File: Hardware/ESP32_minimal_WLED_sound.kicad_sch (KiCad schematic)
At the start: 50 parts, among them J1 Conn_01x04_Male, J2 USB_C_Receptacle_USB2.0, J3 Conn_01x02_Male, J4 Barrel_Jack_Switch_Pin3Ring, J5 Conn_01x03_Male, J6 Conn_01x03_Male, J7 Conn_01x03_Male, J8 Conn_01x02_Male, J9 Conn_01x03_Male, Q1 AO3400A, SW2 Boot, U1 LM1117-5, U2 INA226, U3 LM1117-3.3, U4 TXS0102DCT, U5 ESP32-WROOM-32

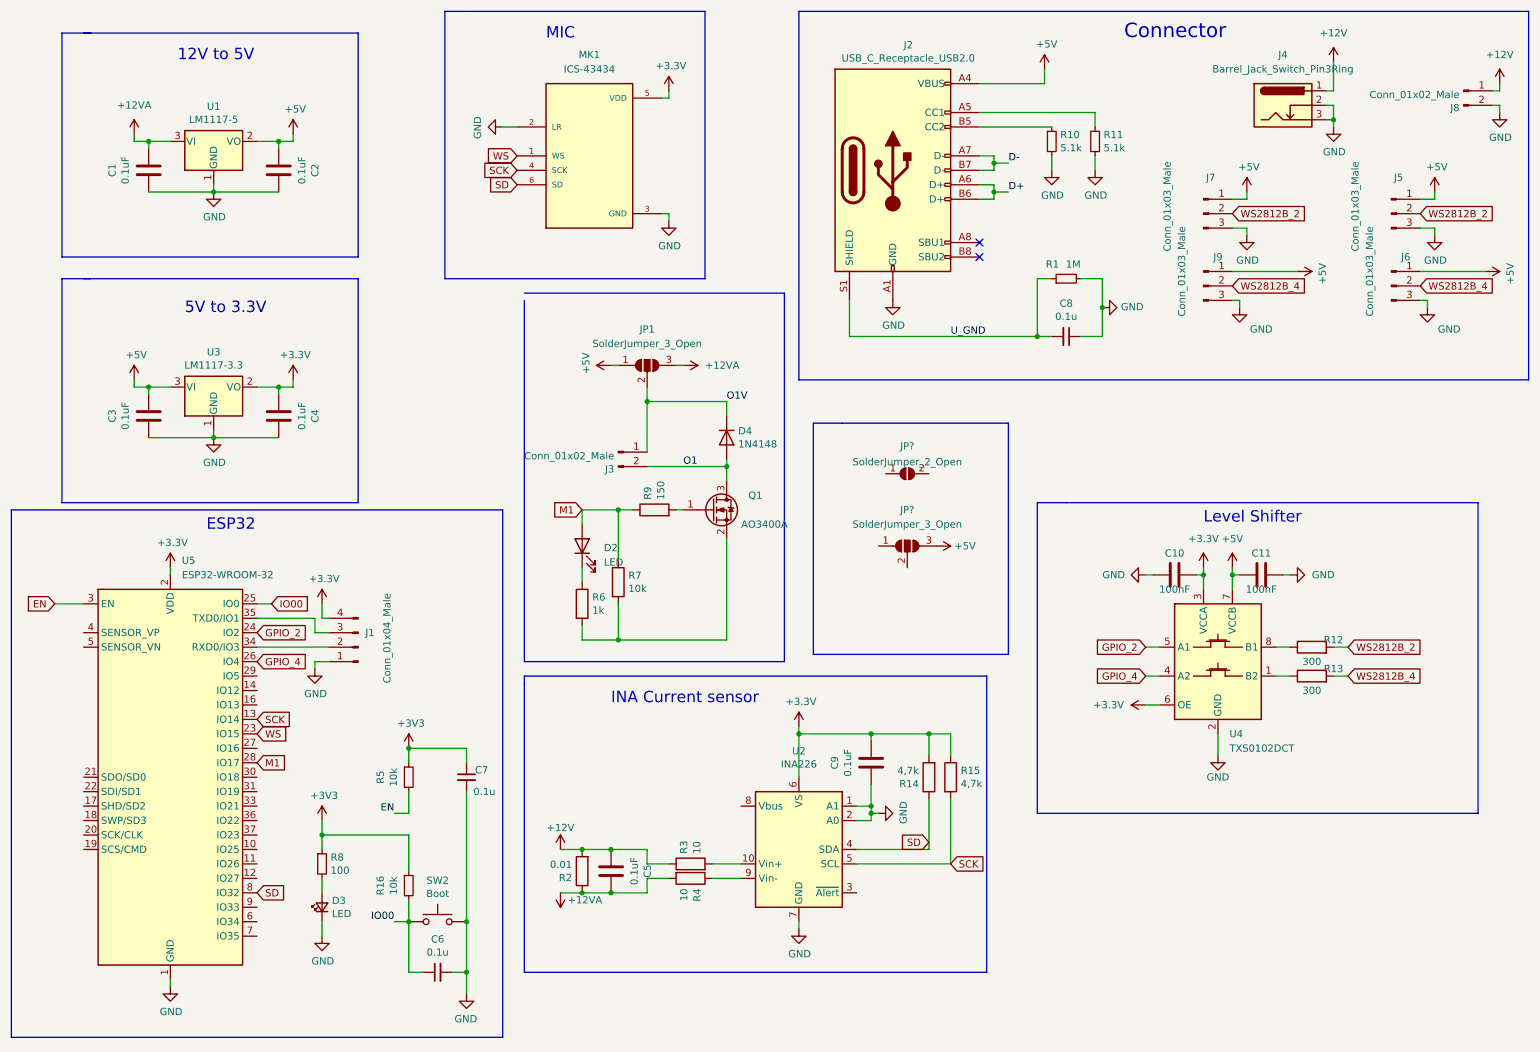
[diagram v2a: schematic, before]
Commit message: switch 12V to 5V to DCDC
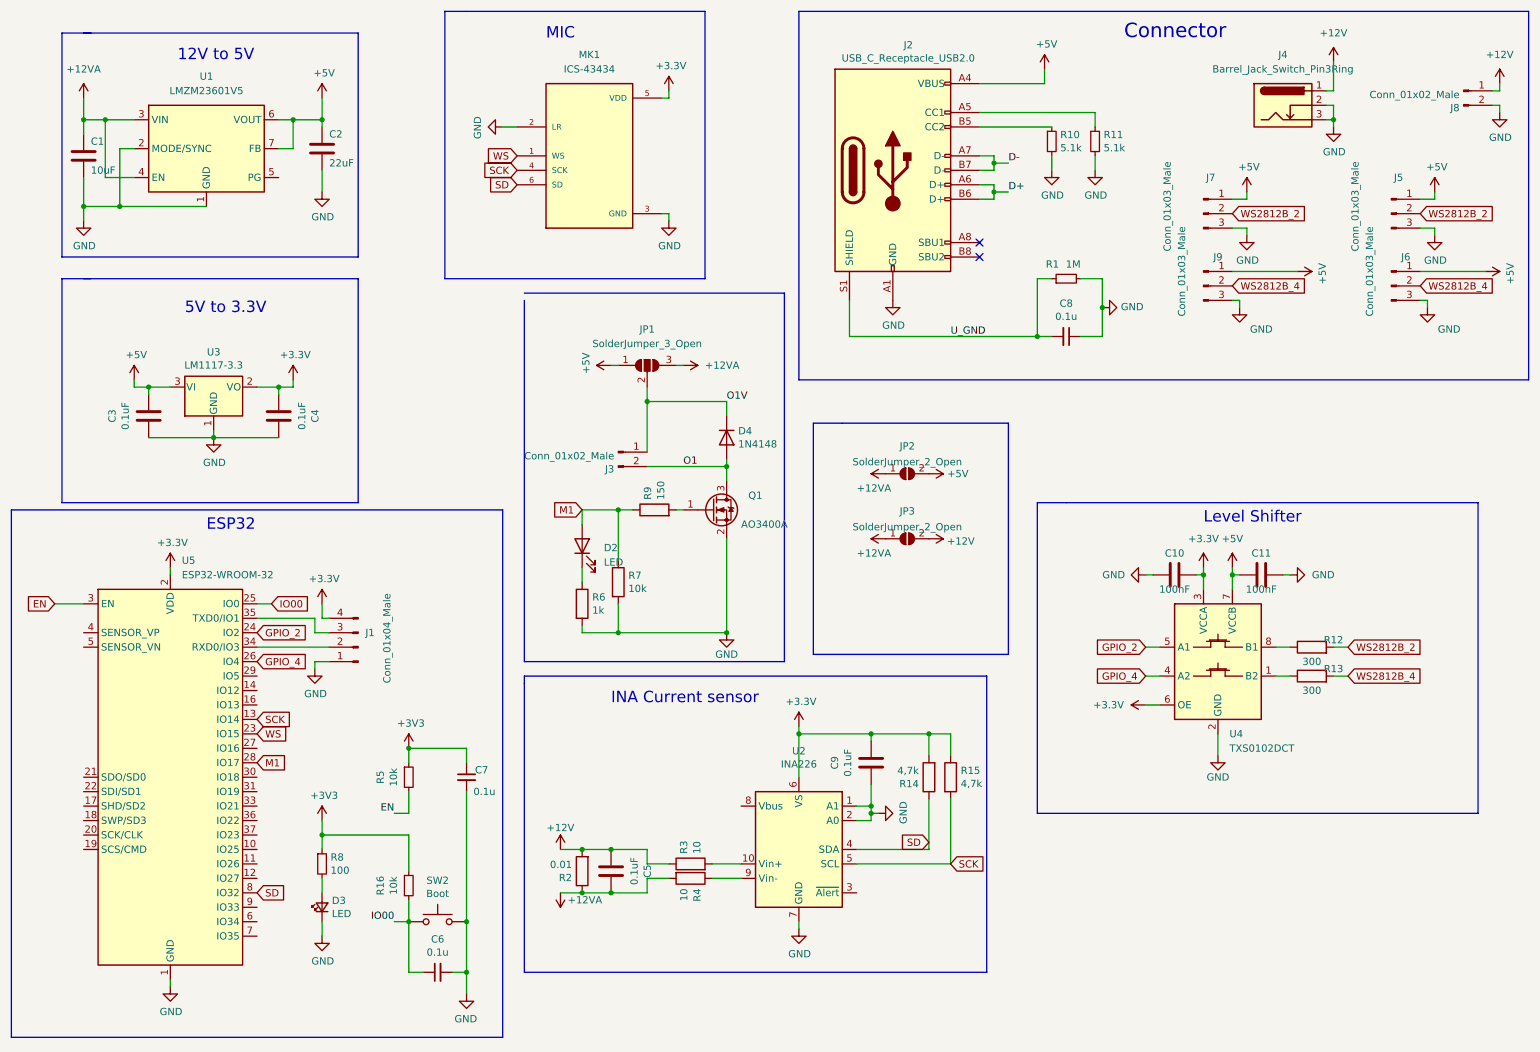
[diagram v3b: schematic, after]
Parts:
- removed JP?: SolderJumper_3_Open, Jumper:SolderJumper-3_P1.3mm_Open_Pad1.0x1.5mm, symbol Jumper:SolderJumper_3_Open
- removed U1: LM1117-5, Package_TO_SOT_SMD:SOT-223, symbol Regulator_Linear:LM1117-3.3
- added JP3: SolderJumper_2_Open, Jumper:SolderJumper-2_P1.3mm_Open_Pad1.0x1.5mm, symbol Jumper:SolderJumper_2_Open
- added U1: LMZM23601V5, Package_LGA:Texas_SIL0010A_MicroSiP-10-1EP_3.8x3mm_P0.6mm_EP0.7x2.9mm_ThermalVias, symbol Regulator_Switching:LMZM23601V5
- C1: value 0.1uF -> 10uF; footprint Capacitor_SMD:C_0805_2012Metric -> Capacitor_SMD:C_0603_1608Metric
- C2: value 0.1uF -> 22uF
- gave numbers to parts that had none: 1
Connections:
- net +12V: now also JP3.2 (B)
- net +12VA: now also JP2.1 (A), JP3.1 (A), U1.3 (VIN), U1.4 (EN)
- net +5V: now also C2.1, JP2.2 (B), U1.6 (VOUT), U1.7 (FB); no longer C2.2
- net GND: now also C2.2, Q1.2 (S), R6.2, R7.2, U1.1 (GND), U1.11 (GND), U1.2 (MODE/SYNC); no longer C2.1

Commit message: update button
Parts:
- removed SW2: Boot, Button_Switch_SMD:SW_SPST_B3U-1000P-B, symbol Switch:SW_Push
- added SW1: SW_Push, Button_Switch_SMD:SW_Push_SPST_NO_Alps_SKRK, symbol Switch:SW_Push
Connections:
- net GND: now also SW1.2
- net IO00: now also SW1.1
